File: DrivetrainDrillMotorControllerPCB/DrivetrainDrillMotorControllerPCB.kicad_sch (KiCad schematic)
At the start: 39 parts, among them J1 DC-005-5A-2.0, J10 Conn_01x02_Socket, J11 Conn_01x02_Socket, J12 Conn_01x02_Socket, J13 Conn_01x02_Socket, J14 Conn_01x02_Socket, J15 Conn_01x02_Socket, J16 Conn_01x02_Socket, J17 Conn_01x08_Socket, J2 Conn_01x02_Socket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

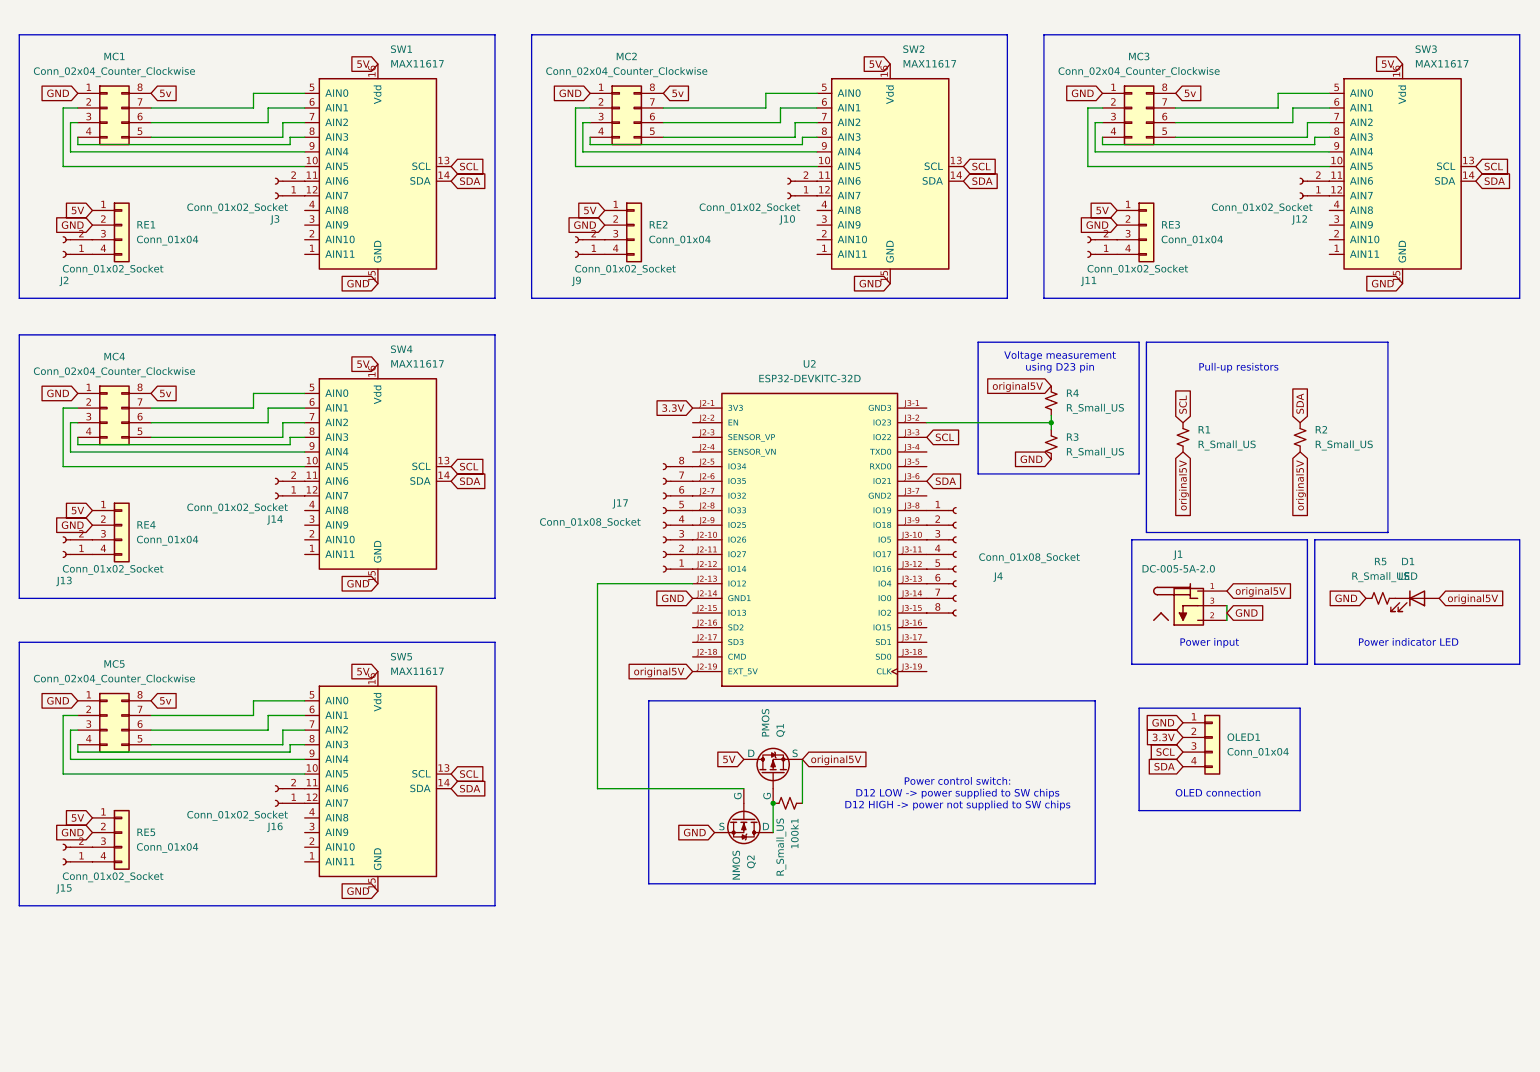
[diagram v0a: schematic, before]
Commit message: Added copper paths to PCB
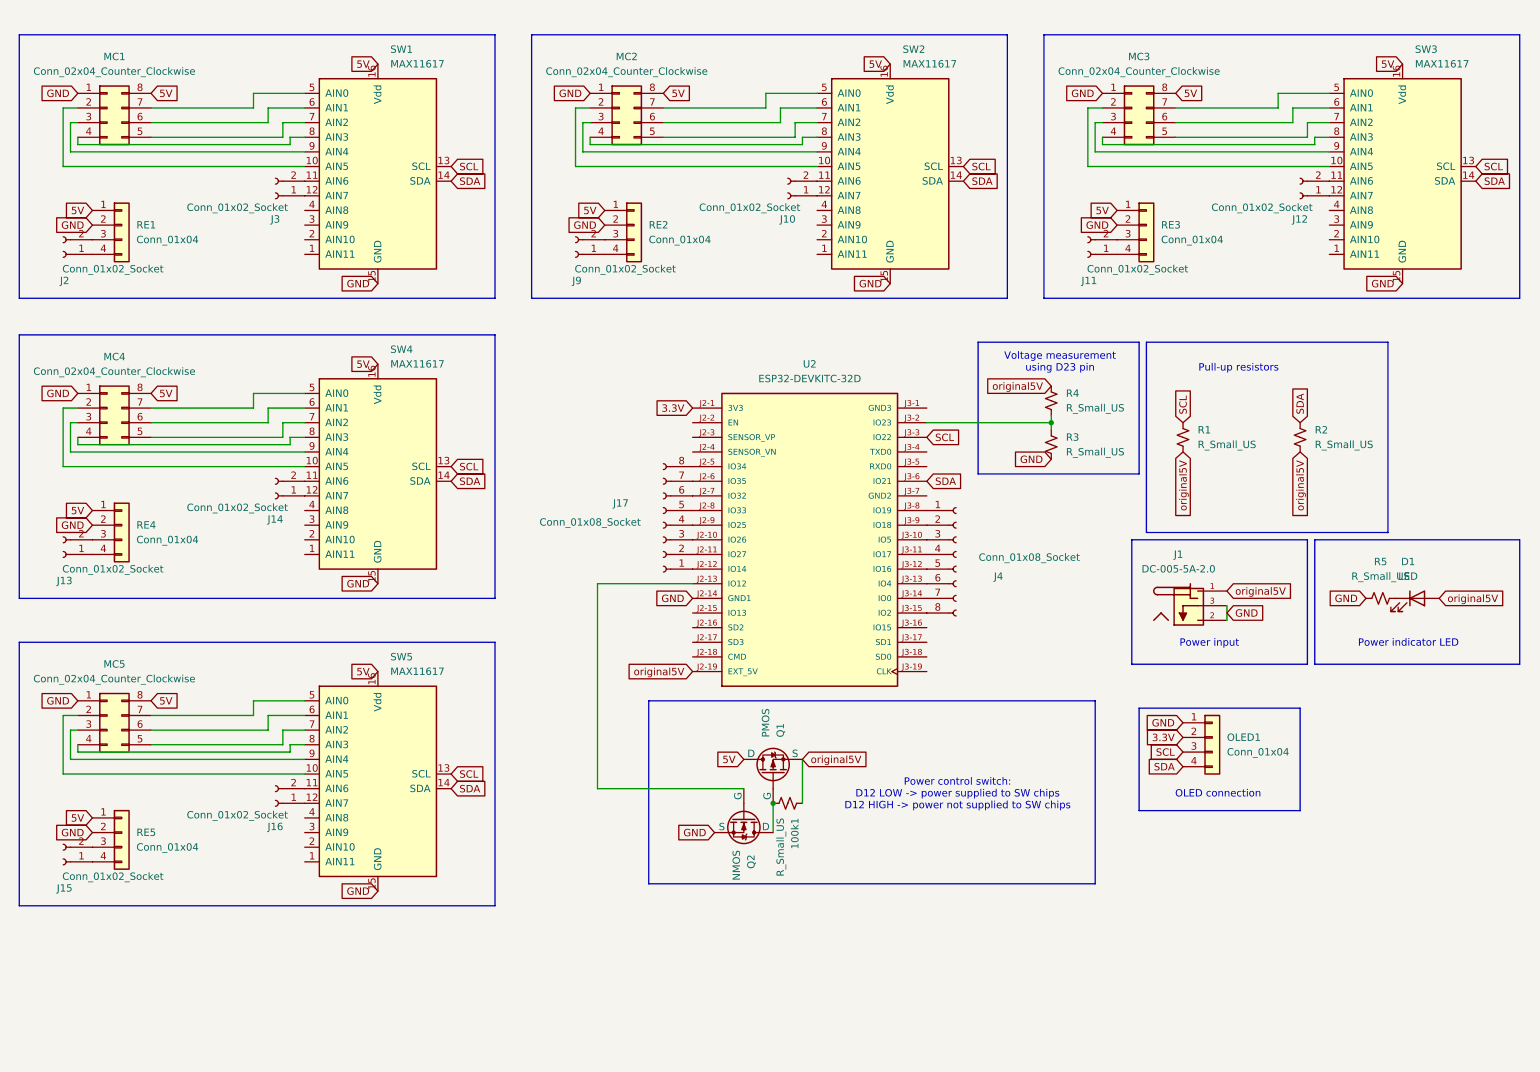
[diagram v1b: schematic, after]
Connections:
- net 5v is gone; now on net 5V: MC1.8 (Pin_8), MC2.8 (Pin_8), MC3.8 (Pin_8), MC4.8 (Pin_8), MC5.8 (Pin_8)
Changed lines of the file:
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@@
 		)
 	)
-	(global_label "5v"
+	(global_label "5V"
 		(shape input)
 		(at 40.64 133.35 0)
@@
 		)
 		(property "Intersheetrefs" "${INTERSHEET_REFS}"
-			(at 45.8023 133.35 0)
+			(at 45.9233 133.35 0)
 			(effects
 				(font
@@
 		)
 	)
-	(global_label "5v"
+	(global_label "5V"
 		(shape input)
 		(at 40.64 80.01 0)
@@
 		)
 		(property "Intersheetrefs" "${INTERSHEET_REFS}"
-			(at 45.8023 80.01 0)
+			(at 45.9233 80.01 0)
 			(effects
 				(font
@@
 		)
 	)
-	(global_label "5v"
+	(global_label "5V"
 		(shape input)
 		(at 218.44 27.94 0)
@@
 		)
 		(property "Intersheetrefs" "${INTERSHEET_REFS}"
-			(at 223.6023 27.94 0)
+			(at 223.7233 27.94 0)
 			(effects
 				(font
@@
 		)
 	)
-	(global_label "5v"
+	(global_label "5V"
 		(shape input)
 		(at 129.54 27.94 0)
@@
 		)
 		(property "Intersheetrefs" "${INTERSHEET_REFS}"
-			(at 134.7023 27.94 0)
+			(at 134.8233 27.94 0)
 			(effects
 				(font
@@
 		)
 	)
-	(global_label "5v"
+	(global_label "5V"
 		(shape input)
 		(at 40.64 27.94 0)
@@
 		)
 		(property "Intersheetrefs" "${INTERSHEET_REFS}"
-			(at 45.8023 27.94 0)
-			(effects
-				(font
+			(at 45.9233 27.94 0)
+			(effects
+				(font

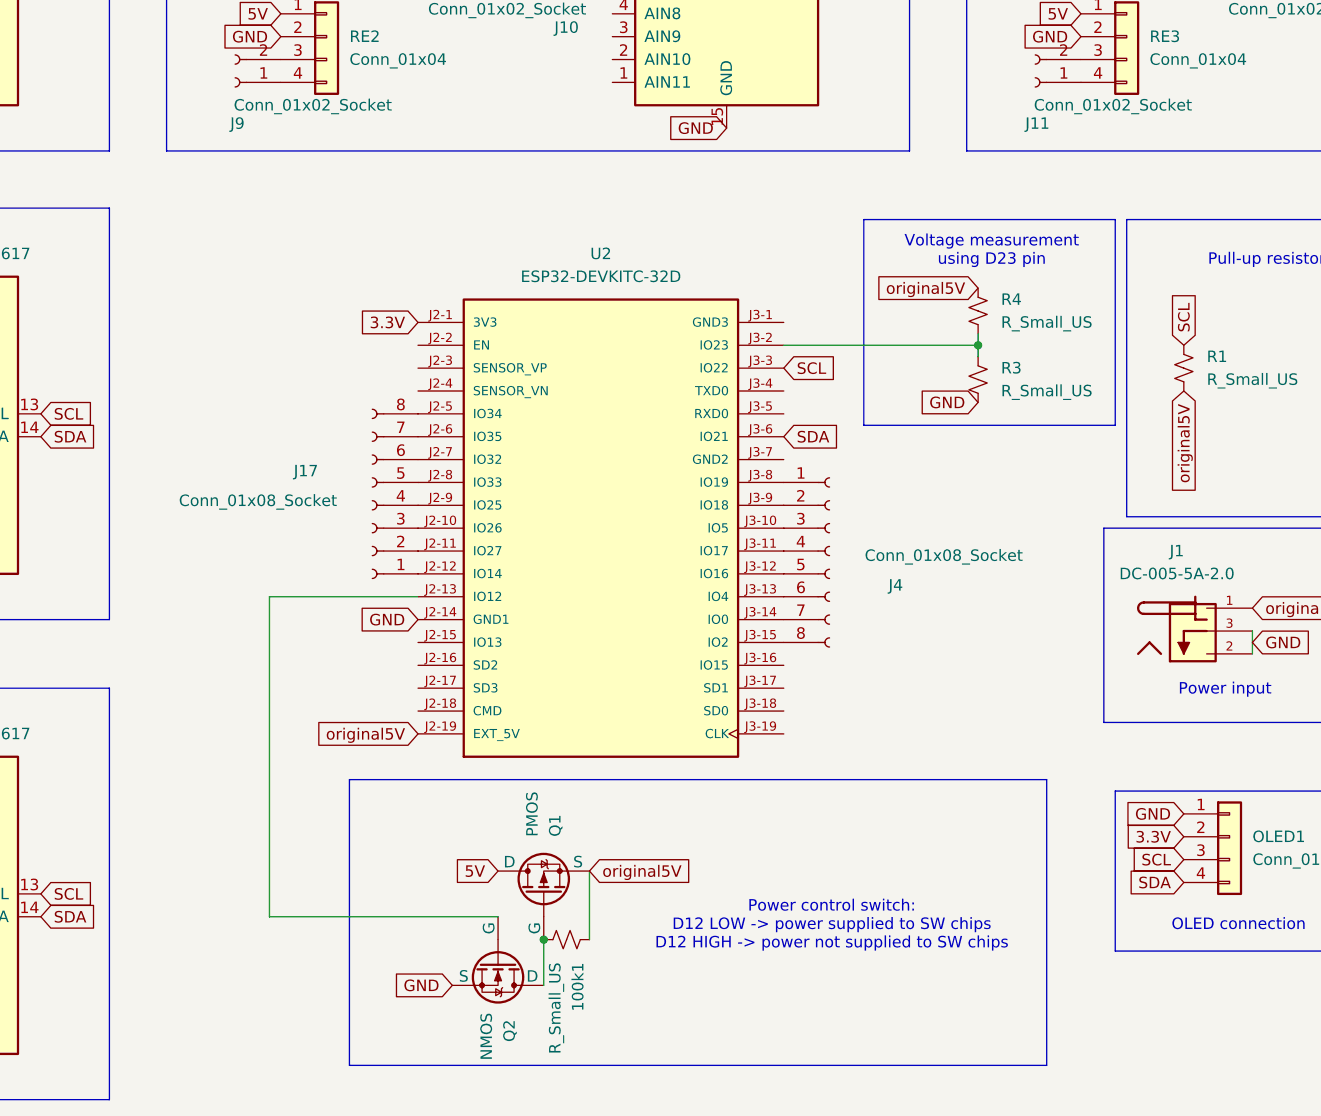
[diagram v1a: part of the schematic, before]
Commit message: Corrected devkit footprint
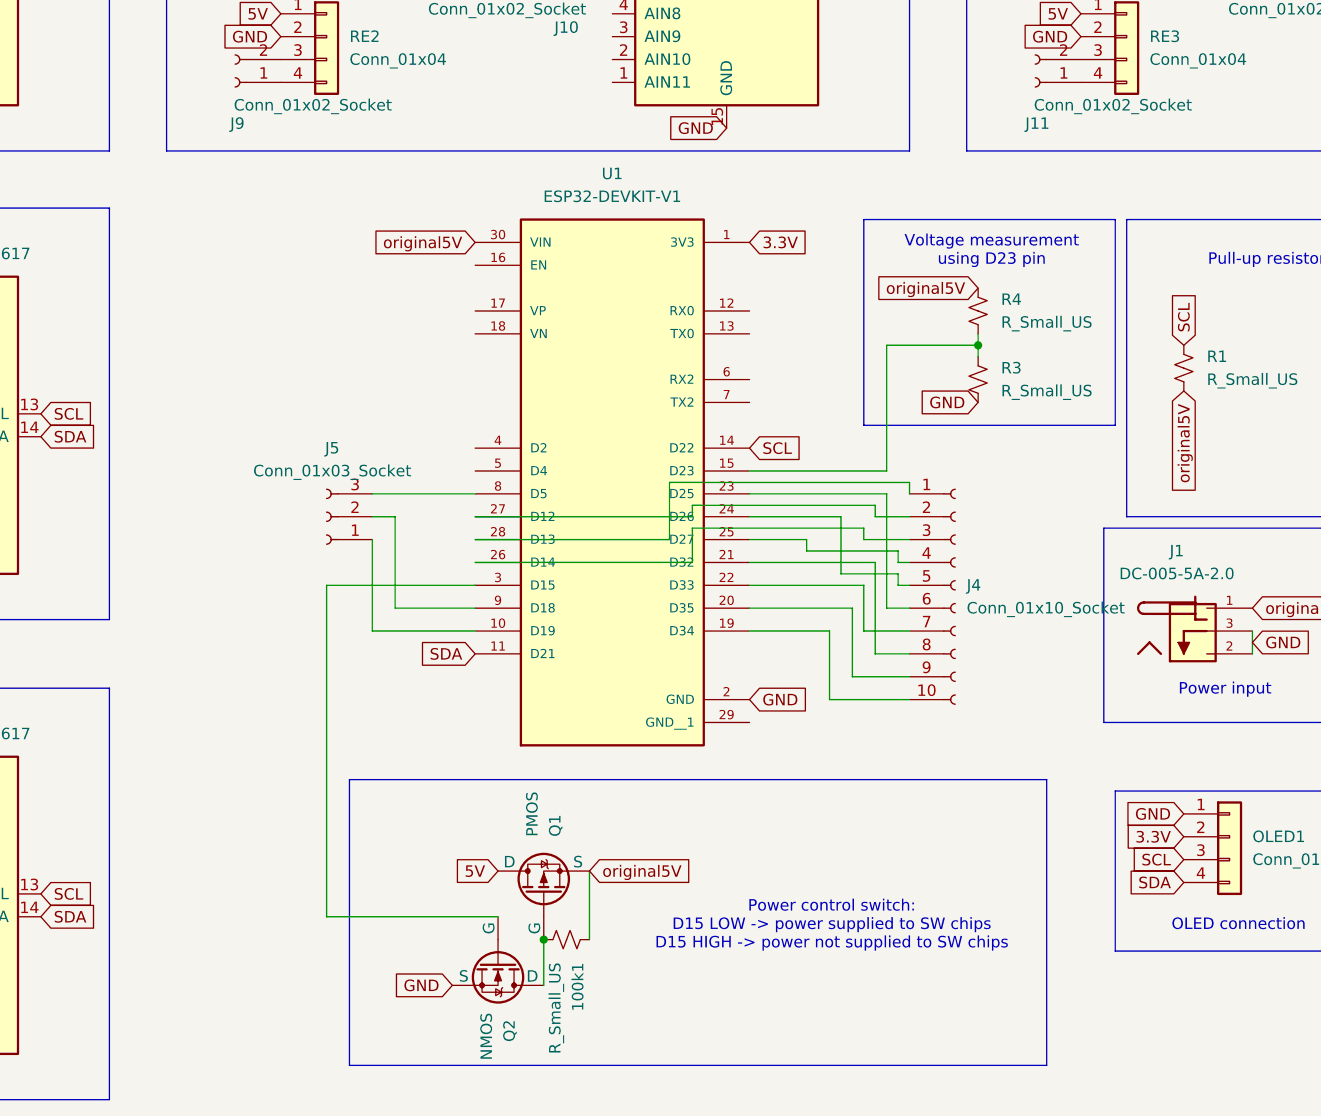
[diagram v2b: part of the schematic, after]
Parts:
- removed J17, J4: Conn_01x08_Socket, Connector_PinHeader_2.54mm:PinHeader_1x08_P2.54mm_Vertical, symbol Connector:Conn_01x08_Socket
- removed U2: ESP32-DEVKITC-32D, ESP32-DEVKITC-32D:MODULE_ESP32-DEVKITC-32D, symbol ESP32-DEVKITC-32D:ESP32-DEVKITC-32D
- added J4: Conn_01x10_Socket, Connector_PinHeader_2.54mm:PinHeader_1x10_P2.54mm_Vertical, symbol Connector:Conn_01x10_Socket
- added J5: Conn_01x03_Socket, Connector_PinHeader_2.54mm:PinHeader_1x03_P2.54mm_Vertical, symbol Connector:Conn_01x03_Socket
- added U1: ESP32-DEVKIT-V1, ESP32-DEVKIT-V1:MODULE_ESP32_DEVKIT_V1, symbol ESP32-DEVKIT-V1:ESP32-DEVKIT-V1
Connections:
- net 3.3V: now also U1.1 (3V3)
- net GND: now also U1.2 (GND)
- net SCL: now also U1.14 (D22)
- net SDA: now also U1.11 (D21)
- net original5V: now also U1.30 (VIN)
- net at Q2.2 (G): now also U1.3 (D15)
- net at R3.1, R4.2: now also U1.15 (D23)
- new net: J5.1 (Pin_1), U1.10 (D19)
- new net: J5.2 (Pin_2), U1.9 (D18)
- new net: J5.3 (Pin_3), U1.8 (D5)
- new net: J4.1 (Pin_1), U1.28 (D13)
- new net: J4.10 (Pin_10), U1.19 (D34)
- new net: J4.2 (Pin_2), U1.27 (D12)
- new net: J4.3 (Pin_3), U1.26 (D14)
- new net: J4.4 (Pin_4), U1.25 (D27)
- new net: J4.5 (Pin_5), U1.24 (D26)
- new net: J4.6 (Pin_6), U1.23 (D25)
- new net: J4.7 (Pin_7), U1.22 (D33)
- new net: J4.8 (Pin_8), U1.21 (D32)
- new net: J4.9 (Pin_9), U1.20 (D35)
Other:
- note added: "Power control switch: D15 LOW -> power supplied to SW chips D15 HIGH -> power not supplied to SW chips"
- note removed: "Power control switch: D12 LOW -> power supplied to SW chips D12 HIGH -> power not supplied to SW chips"

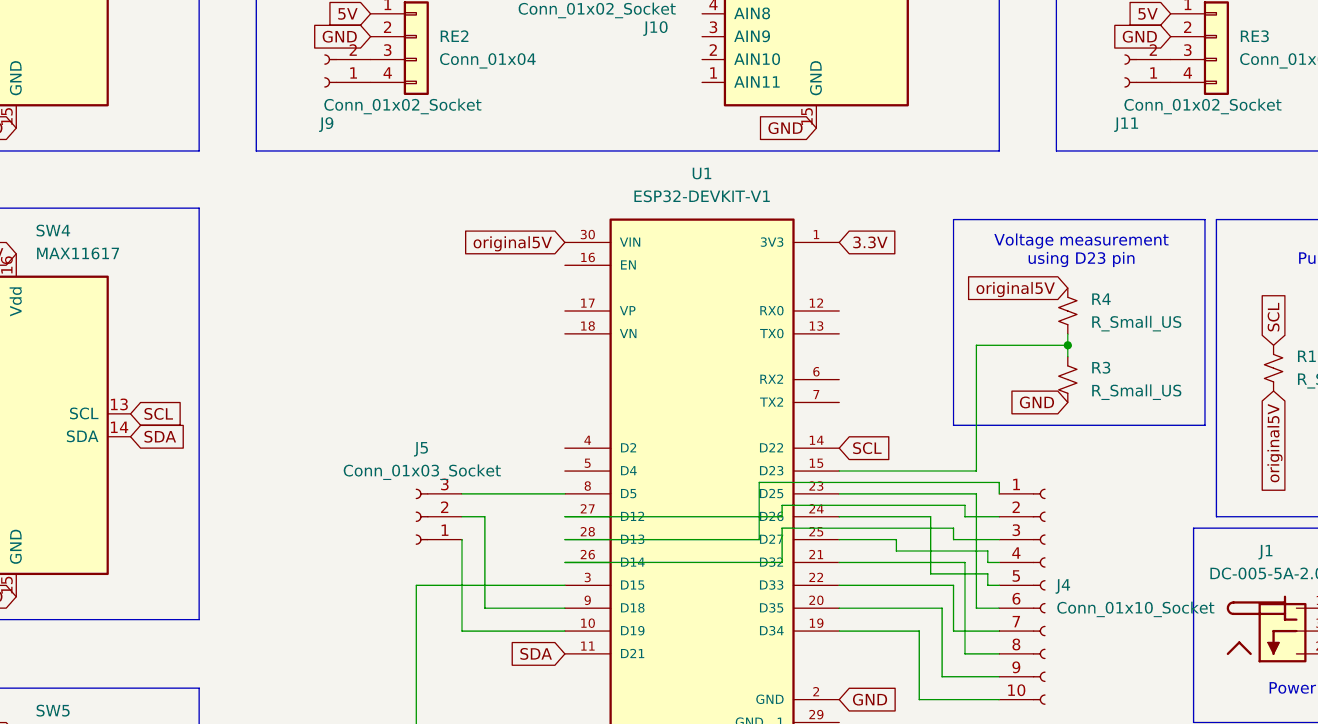
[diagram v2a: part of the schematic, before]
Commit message: made esp32 power from battery optional
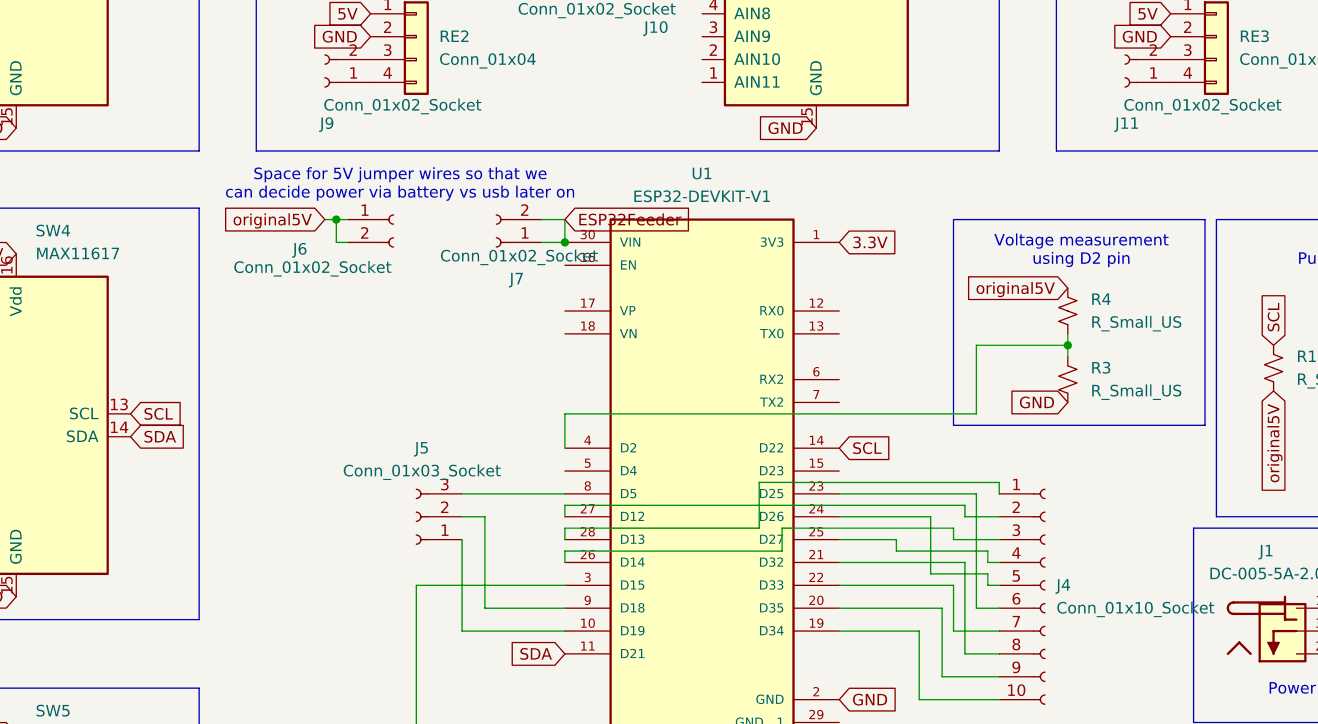
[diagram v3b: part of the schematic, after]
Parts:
- added J6, J7: Conn_01x02_Socket, Connector_PinHeader_2.54mm:PinHeader_1x02_P2.54mm_Vertical, symbol Connector:Conn_01x02_Socket
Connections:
- net original5V: now also J6.1 (Pin_1), J6.2 (Pin_2); no longer U1.30 (VIN)
- net at R3.1, R4.2: now also U1.4 (D2); no longer U1.15 (D23)
- new net ESP32Feeder: J7.1 (Pin_1), J7.2 (Pin_2), U1.30 (VIN)
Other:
- note added: "Space for 5V jumper wires so that we can decide power via battery vs usb later on"
- note added: "Voltage measurement using D2 pin"
- note removed: "Voltage measurement using D23 pin"

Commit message: Added linear regulator
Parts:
- removed J7: Conn_01x02_Socket, Connector_PinHeader_2.54mm:PinHeader_1x02_P2.54mm_Vertical, symbol Connector:Conn_01x02_Socket
- added J7: Conn_01x03_Pin, Connector_PinHeader_2.54mm:PinHeader_1x03_P2.54mm_Vertical, symbol Connector:Conn_01x03_Pin
- added U3: L7805, Connector_PinHeader_2.54mm:PinHeader_1x03_P2.54mm_Vertical, symbol Regulator_Linear:L7805
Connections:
- net ESP32Feeder: now also J6.2 (Pin_2)
- net GND: now also U3.2 (GND)
- net original5V: now also J7.3 (Pin_3), U3.3 (OUT); no longer J1.1, J6.2 (Pin_2), R4.1
- new net: J7.1 (Pin_1), U3.1 (IN)
- new net Vin: J1.1, J7.2 (Pin_2), R4.1
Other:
- note added: "<< Pin allows for switching between linear regulator 12V input) and 5V input modes"
- note added: "Space for 5V jumper so that we can decide power via battery vs usb later on"
- note removed: "Space for 5V jumper wires so that we can decide power via battery vs usb later on"

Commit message: Final
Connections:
- net 3.3V: now also R1.2, R2.2
- net original5V: no longer R1.2, R2.2
